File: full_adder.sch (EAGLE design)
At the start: 69 parts, among them IC1 SN74LS74AN, IC2 NE555, IC3 CD4052BE, IC4 CD4052BE, IC5 CD4052BE, IC6 74HC4051N,652

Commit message: reverse polarity protection added
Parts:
- added GND_IN, VCC_IN: LSP11, solpad:LSP11
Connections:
- new net N$30: VCC_IN.MP
- net GND: now also GND_IN.MP
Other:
- note added: "10 Reverse Polarity Protection"
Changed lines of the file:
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@@
 <part name="R21" library="rcl" library_urn="urn:adsk.eagle:library:334" deviceset="R-EU_" device="R1206" package3d_urn="urn:adsk.eagle:package:23540/2" value="1k"/>
 <part name="R22" library="rcl" library_urn="urn:adsk.eagle:library:334" deviceset="R-EU_" device="R1206" package3d_urn="urn:adsk.eagle:package:23540/2" value="1k"/>
+<part name="FRAME1" library="frames" library_urn="urn:adsk.eagle:library:229" deviceset="A3L-LOC" device=""/>
+<part name="VCC_IN" library="solpad" library_urn="urn:adsk.eagle:library:364" deviceset="LSP11" device="" package3d_urn="urn:adsk.eagle:package:26502/1"/>
+<part name="GND_IN" library="solpad" library_urn="urn:adsk.eagle:library:364" deviceset="LSP11" device="" package3d_urn="urn:adsk.eagle:package:26502/1"/>
+<part name="GND47" library="supply1" library_urn="urn:adsk.eagle:library:371" deviceset="GND" device=""/>
+<part name="Q1" library="transistor-power" library_urn="urn:adsk.eagle:library:400" deviceset="P-MOSFET_SYMBOL" device=""/>
 </parts>
 <sheets>
@@
 </segment>
 </net>
+</nets>
+</sheet>
+<sheet>
+<plain>
+<text x="-177.8" y="190.5" size="3.81" layer="100">10 Reverse Polarity Protection</text>
+</plain>
+<instances>
+<instance part="FRAME1" gate="G$1" x="-187.96" y="-55.88" smashed="yes">
+<attribute name="DRAWING_NAME" x="156.21" y="-40.64" size="2.54" layer="94"/>
+<attribute name="LAST_DATE_TIME" x="156.21" y="-45.72" size="2.286" layer="94"/>
+<attribute name="SHEET" x="169.545" y="-50.8" size="2.54" layer="94"/>
+</instance>
+<instance part="VCC_IN" gate="1" x="-170.18" y="177.8" smashed="yes" rot="R90">
+<attribute name="NAME" x="-168.91" y="182.499" size="1.778" layer="95" rot="R180"/>
+</instance>
+<instance part="GND_IN" gate="1" x="-170.18" y="162.56" smashed="yes" rot="R90">
+<attribute name="NAME" x="-168.91" y="167.259" size="1.778" layer="95" rot="R180"/>
+</instance>
+<instance part="GND47" gate="1" x="-149.86" y="157.48" smashed="yes">
+<attribute name="VALUE" x="-152.4" y="154.94" size="1.778" layer="96"/>
+</instance>
+<instance part="Q1" gate="G$1" x="-152.4" y="175.26" smashed="yes" rot="MR90">
+<attribute name="NAME" x="-152.4" y="182.88" size="1.778" layer="95" rot="MR180"/>
+<attribute name="VALUE" x="-152.4" y="185.42" size="1.778" layer="96" rot="MR180"/>
+</instance>
+</instances>
+<busses>
+</busses>
+<nets>
+<net name="N$30" class="0">
+<segment>
+<pinref part="VCC_IN" gate="1" pin="MP"/>
+<wire x1="-167.64" y1="177.8" x2="-157.48" y2="177.8" width="0.1524" layer="91"/>
+</segment>
+</net>
+<net name="VCC" class="0">
+<segment>
+<wire x1="-147.32" y1="177.8" x2="-144.78" y2="177.8" width="0.1524" layer="91"/>
+<label x="-144.78" y="177.8" size="1.016" layer="95" xref="yes"/>
+</segment>
+</net>
+<net name="GND" class="0">
+<segment>
+<pinref part="GND_IN" gate="1" pin="MP"/>
+<wire x1="-149.86" y1="172.72" x2="-149.86" y2="162.56" width="0.1524" layer="91"/>
+<wire x1="-149.86" y1="162.56" x2="-167.64" y2="162.56" width="0.1524" layer="91"/>
+<pinref part="GND47" gate="1" pin="GND"/>
+<wire x1="-149.86" y1="160.02" x2="-149.86" y2="162.56" width="0.1524" layer="91"/>
+<junction x="-149.86" y="162.56"/>
+</segment>
+</net>

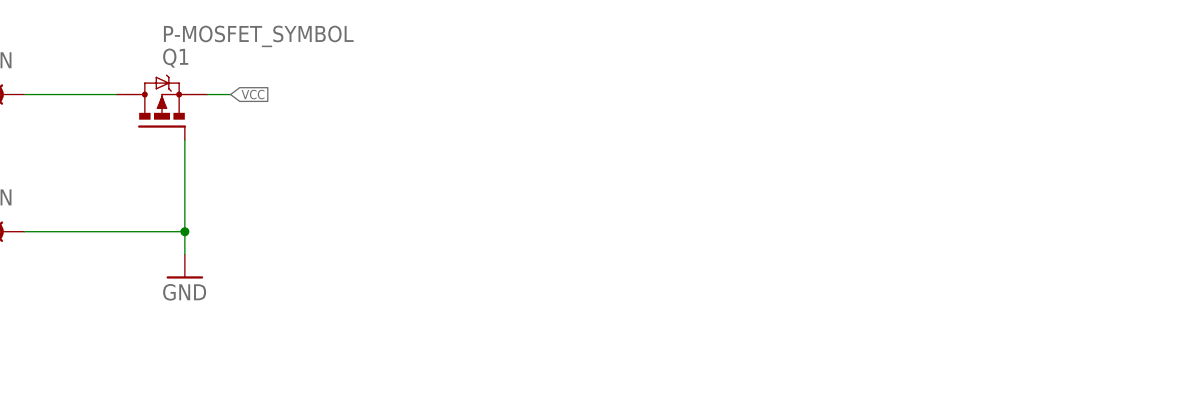
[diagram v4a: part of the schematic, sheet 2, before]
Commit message: basic input protection concept added
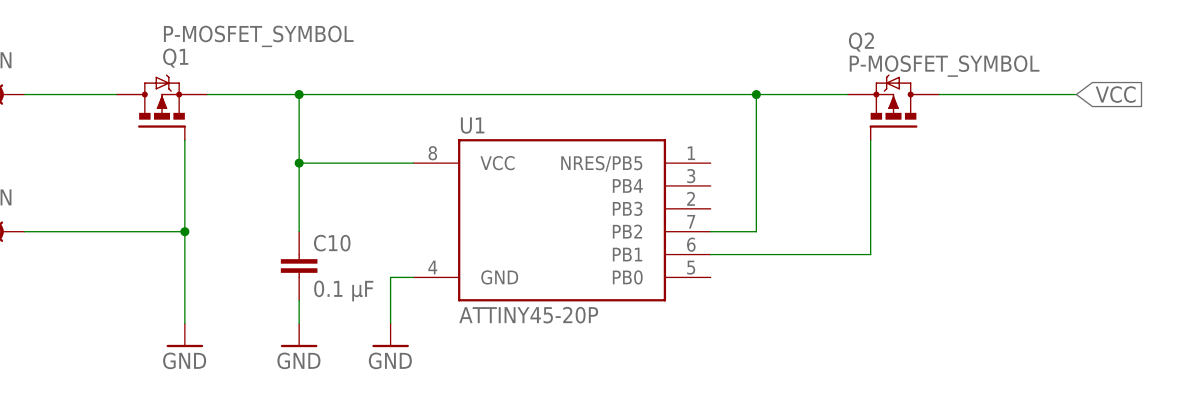
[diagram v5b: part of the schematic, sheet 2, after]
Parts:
- added C10: 0.1 µF, rcl:C-EU025-024X044
- added U1: ATTINY45-20P, _hhn_attiny25_45_85:ATTINY45-20P
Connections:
- new net N$31: C10.1, U1.PB2, U1.VCC
- new net N$32: U1.PB1
- net GND: now also C10.2, U1.GND
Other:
- note added: "10 Reverse Polarity + Overdischarge Protection"
- note removed: "10 Reverse Polarity Protection"
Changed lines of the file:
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@@
 <part name="GND47" library="supply1" library_urn="urn:adsk.eagle:library:371" deviceset="GND" device=""/>
 <part name="Q1" library="transistor-power" library_urn="urn:adsk.eagle:library:400" deviceset="P-MOSFET_SYMBOL" device=""/>
+<part name="U1" library="_hhn_attiny25_45_85" deviceset="ATTINY45*" device="P" technology="-20"/>
+<part name="GND48" library="supply1" library_urn="urn:adsk.eagle:library:371" deviceset="GND" device=""/>
+<part name="C10" library="rcl" library_urn="urn:adsk.eagle:library:334" deviceset="C-EU" device="025-024X044" package3d_urn="urn:adsk.eagle:package:23630/1" value="0.1 µF"/>
+<part name="GND49" library="supply1" library_urn="urn:adsk.eagle:library:371" deviceset="GND" device=""/>
+<part name="Q2" library="transistor-power" library_urn="urn:adsk.eagle:library:400" deviceset="P-MOSFET_SYMBOL" device=""/>
 </parts>
 <sheets>
@@
 <sheet>
 <plain>
-<text x="-177.8" y="190.5" size="3.81" layer="100">10 Reverse Polarity Protection</text>
+<text x="-177.8" y="190.5" size="3.81" layer="100">10 Reverse Polarity + Overdischarge Protection</text>
 </plain>
 <instances>
@@
 <attribute name="NAME" x="-168.91" y="167.259" size="1.778" layer="95" rot="R180"/>
 </instance>
-<instance part="GND47" gate="1" x="-149.86" y="157.48" smashed="yes">
-<attribute name="VALUE" x="-152.4" y="154.94" size="1.778" layer="96"/>
+<instance part="GND47" gate="1" x="-149.86" y="149.86" smashed="yes">
+<attribute name="VALUE" x="-152.4" y="147.32" size="1.778" layer="96"/>
 </instance>
 <instance part="Q1" gate="G$1" x="-152.4" y="175.26" smashed="yes" rot="MR90">
 <attribute name="NAME" x="-152.4" y="182.88" size="1.778" layer="95" rot="MR180"/>
 <attribute name="VALUE" x="-152.4" y="185.42" size="1.778" layer="96" rot="MR180"/>
+</instance>
+<instance part="U1" gate="G$1" x="-109.22" y="165.1" smashed="yes">
+<attribute name="NAME" x="-119.38" y="173.482" size="1.778" layer="95"/>
+<attribute name="VALUE" x="-119.38" y="152.4" size="1.778" layer="96"/>
+</instance>
+<instance part="GND48" gate="1" x="-127" y="149.86" smashed="yes">
+<attribute name="VALUE" x="-129.54" y="147.32" size="1.778" layer="96"/>
+</instance>
+<instance part="C10" gate="G$1" x="-137.16" y="160.02" smashed="yes">
+<attribute name="NAME" x="-135.636" y="160.401" size="1.778" layer="95"/>
+<attribute name="VALUE" x="-135.636" y="155.321" size="1.778" layer="96"/>
+</instance>
+<instance part="GND49" gate="1" x="-137.16" y="149.86" smashed="yes">
+<attribute name="VALUE" x="-139.7" y="147.32" size="1.778" layer="96"/>
+</instance>
+<instance part="Q2" gate="G$1" x="-71.12" y="175.26" smashed="yes" rot="R90">
+<attribute name="NAME" x="-76.2" y="182.88" size="1.778" layer="95"/>
+<attribute name="VALUE" x="-76.2" y="180.34" size="1.778" layer="96"/>
 </instance>
 </instances>
@@
 </segment>
 </net>
-<net name="VCC" class="0">
-<segment>
-<wire x1="-147.32" y1="177.8" x2="-144.78" y2="177.8" width="0.1524" layer="91"/>
-<label x="-144.78" y="177.8" size="1.016" layer="95" xref="yes"/>
-</segment>
-</net>
 <net name="GND" class="0">
 <segment>
@@
 <wire x1="-149.86" y1="162.56" x2="-167.64" y2="162.56" width="0.1524" layer="91"/>
 <pinref part="GND47" gate="1" pin="GND"/>
-<wire x1="-149.86" y1="160.02" x2="-149.86" y2="162.56" width="0.1524" layer="91"/>
+<wire x1="-149.86" y1="152.4" x2="-149.86" y2="162.56" width="0.1524" layer="91"/>
 <junction x="-149.86" y="162.56"/>
 </segment>
-</net>
+<segment>
+<pinref part="U1" gate="G$1" pin="GND"/>
+<wire x1="-124.46" y1="157.48" x2="-127" y2="157.48" width="0.1524" layer="91"/>
+<wire x1="-127" y1="157.48" x2="-127" y2="152.4" width="0.1524" layer="91"/>
+<pinref part="GND48" gate="1" pin="GND"/>
+</segment>
+<segment>
+<pinref part="GND49" gate="1" pin="GND"/>
+<pinref part="C10" gate="G$1" pin="2"/>
+<wire x1="-137.16" y1="152.4" x2="-137.16" y2="154.94" width="0.1524" layer="91"/>
+</segment>
+</net>
+<net name="N$31" class="0">
+<segment>
+<wire x1="-147.32" y1="177.8" x2="-137.16" y2="177.8" width="0.1524" layer="91"/>
+<pinref part="U1" gate="G$1" pin="VCC"/>
+<wire x1="-137.16" y1="177.8" x2="-137.16" y2="170.18" width="0.1524" layer="91"/>
+<wire x1="-137.16" y1="170.18" x2="-124.46" y2="170.18" width="0.1524" layer="91"/>
+<wire x1="-137.16" y1="177.8" x2="-86.36" y2="177.8" width="0.1524" layer="91"/>
+<wire x1="-86.36" y1="177.8" x2="-86.36" y2="162.56" width="0.1524" layer="91"/>
+<junction x="-137.16" y="177.8"/>
+<pinref part="U1" gate="G$1" pin="PB2"/>
+<wire x1="-86.36" y1="162.56" x2="-91.44" y2="162.56" width="0.1524" layer="91"/>
+<pinref part="C10" gate="G$1" pin="1"/>
+<wire x1="-137.16" y1="162.56" x2="-137.16" y2="170.18" width="0.1524" layer="91"/>
+<junction x="-137.16" y="170.18"/>
+<wire x1="-86.36" y1="177.8" x2="-76.2" y2="177.8" width="0.1524" layer="91"/>
+<junction x="-86.36" y="177.8"/>
+</segment>
+</net>
+<net name="N$32" class="0">
+<segment>
+<pinref part="U1" gate="G$1" pin="PB1"/>
+<wire x1="-91.44" y1="160.02" x2="-73.66" y2="160.02" width="0.1524" layer="91"/>
+<wire x1="-73.66" y1="172.72" x2="-73.66" y2="160.02" width="0.1524" layer="91"/>
+</segment>
+</net>
+<net name="VCC" class="0">
+<segment>
+<wire x1="-66.04" y1="177.8" x2="-50.8" y2="177.8" width="0.1524" layer="91"/>
+<label x="-50.8" y="177.8" size="1.778" layer="95" xref="yes"/>
+</segment>
+</net>

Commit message: minor fixes
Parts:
- added LED13: (no value), led:LED5MM
- added R23: 10k, rcl:R-EU_R1206
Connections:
- new net N$33: LED13.A, R23.1
- new net N$34: R23.2, U1.PB2
- net GND: now also LED13.C
- net N$31: no longer U1.PB2
- net N$32: now also U1.PB4; no longer U1.PB1
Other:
- note added: "small led"
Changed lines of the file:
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@@
 <part name="C10" library="rcl" library_urn="urn:adsk.eagle:library:334" deviceset="C-EU" device="025-024X044" package3d_urn="urn:adsk.eagle:package:23630/1" value="0.1 µF"/>
 <part name="GND49" library="supply1" library_urn="urn:adsk.eagle:library:371" deviceset="GND" device=""/>
-<part name="Q2" library="transistor-power" library_urn="urn:adsk.eagle:library:400" deviceset="P-MOSFET_SYMBOL" device=""/>
+<part name="Q3" library="transistor-power" library_urn="urn:adsk.eagle:library:400" deviceset="N-MOSFET_SYMBOL" device=""/>
+<part name="LED13" library="led" library_urn="urn:adsk.eagle:library:259" deviceset="LED" device="5MM" package3d_urn="urn:adsk.eagle:package:15799/2"/>
+<part name="R23" library="rcl" library_urn="urn:adsk.eagle:library:334" deviceset="R-EU_" device="R1206" package3d_urn="urn:adsk.eagle:package:23540/2" value="10k"/>
+<part name="GND50" library="supply1" library_urn="urn:adsk.eagle:library:371" deviceset="GND" device=""/>
 </parts>
 <sheets>
@@
 <plain>
 <text x="-177.8" y="190.5" size="3.81" layer="100">10 Reverse Polarity + Overdischarge Protection</text>
+<text x="-73.66" y="144.78" size="1.778" layer="97">small led</text>
 </plain>
 <instances>
@@
 <attribute name="NAME" x="-168.91" y="167.259" size="1.778" layer="95" rot="R180"/>
 </instance>
-<instance part="GND47" gate="1" x="-149.86" y="149.86" smashed="yes">
-<attribute name="VALUE" x="-152.4" y="147.32" size="1.778" layer="96"/>
+<instance part="GND47" gate="1" x="-149.86" y="139.7" smashed="yes">
+<attribute name="VALUE" x="-152.4" y="137.16" size="1.778" layer="96"/>
 </instance>
 <instance part="Q1" gate="G$1" x="-152.4" y="175.26" smashed="yes" rot="MR90">
@@
 <attribute name="VALUE" x="-119.38" y="152.4" size="1.778" layer="96"/>
 </instance>
-<instance part="GND48" gate="1" x="-127" y="149.86" smashed="yes">
-<attribute name="VALUE" x="-129.54" y="147.32" size="1.778" layer="96"/>
+<instance part="GND48" gate="1" x="-127" y="139.7" smashed="yes">
+<attribute name="VALUE" x="-129.54" y="137.16" size="1.778" layer="96"/>
 </instance>
 <instance part="C10" gate="G$1" x="-137.16" y="160.02" smashed="yes">
@@
 <attribute name="VALUE" x="-135.636" y="155.321" size="1.778" layer="96"/>
 </instance>
-<instance part="GND49" gate="1" x="-137.16" y="149.86" smashed="yes">
-<attribute name="VALUE" x="-139.7" y="147.32" size="1.778" layer="96"/>
-</instance>
-<instance part="Q2" gate="G$1" x="-71.12" y="175.26" smashed="yes" rot="R90">
-<attribute name="NAME" x="-76.2" y="182.88" size="1.778" layer="95"/>
-<attribute name="VALUE" x="-76.2" y="180.34" size="1.778" layer="96"/>
+<instance part="GND49" gate="1" x="-137.16" y="139.7" smashed="yes">
+<attribute name="VALUE" x="-139.7" y="137.16" size="1.778" layer="96"/>
+</instance>
+<instance part="Q3" gate="G$1" x="-81.28" y="175.26" smashed="yes" rot="R90">
+<attribute name="NAME" x="-86.36" y="182.88" size="1.778" layer="95"/>
+<attribute name="VALUE" x="-86.36" y="180.34" size="1.778" layer="96"/>
+</instance>
+<instance part="LED13" gate="G$1" x="-78.74" y="147.32" smashed="yes">
+<attribute name="NAME" x="-75.184" y="142.748" size="1.778" layer="95" rot="R90"/>
+<attribute name="VALUE" x="-73.025" y="142.748" size="1.778" layer="96" rot="R90"/>
+</instance>
+<instance part="R23" gate="G$1" x="-78.74" y="154.94" smashed="yes" rot="R90">
+<attribute name="NAME" x="-77.47" y="156.4386" size="1.778" layer="95"/>
+<attribute name="VALUE" x="-77.47" y="154.178" size="1.778" layer="96"/>
+</instance>
+<instance part="GND50" gate="1" x="-78.74" y="139.7" smashed="yes">
+<attribute name="VALUE" x="-81.28" y="137.16" size="1.778" layer="96"/>
 </instance>
 </instances>
@@
 <wire x1="-149.86" y1="162.56" x2="-167.64" y2="162.56" width="0.1524" layer="91"/>
 <pinref part="GND47" gate="1" pin="GND"/>
-<wire x1="-149.86" y1="152.4" x2="-149.86" y2="162.56" width="0.1524" layer="91"/>
+<wire x1="-149.86" y1="142.24" x2="-149.86" y2="162.56" width="0.1524" layer="91"/>
 <junction x="-149.86" y="162.56"/>
 </segment>
@@
 <pinref part="U1" gate="G$1" pin="GND"/>
 <wire x1="-124.46" y1="157.48" x2="-127" y2="157.48" width="0.1524" layer="91"/>
-<wire x1="-127" y1="157.48" x2="-127" y2="152.4" width="0.1524" layer="91"/>
+<wire x1="-127" y1="157.48" x2="-127" y2="142.24" width="0.1524" layer="91"/>
 <pinref part="GND48" gate="1" pin="GND"/>
 </segment>
@@
 <pinref part="GND49" gate="1" pin="GND"/>
 <pinref part="C10" gate="G$1" pin="2"/>
-<wire x1="-137.16" y1="152.4" x2="-137.16" y2="154.94" width="0.1524" layer="91"/>
+<wire x1="-137.16" y1="142.24" x2="-137.16" y2="154.94" width="0.1524" layer="91"/>
+</segment>
+<segment>
+<pinref part="GND50" gate="1" pin="GND"/>
+<pinref part="LED13" gate="G$1" pin="C"/>
 </segment>
 </net>
@@
 <wire x1="-137.16" y1="170.18" x2="-124.46" y2="170.18" width="0.1524" layer="91"/>
 <wire x1="-137.16" y1="177.8" x2="-86.36" y2="177.8" width="0.1524" layer="91"/>
-<wire x1="-86.36" y1="177.8" x2="-86.36" y2="162.56" width="0.1524" layer="91"/>
 <junction x="-137.16" y="177.8"/>
-<pinref part="U1" gate="G$1" pin="PB2"/>
-<wire x1="-86.36" y1="162.56" x2="-91.44" y2="162.56" width="0.1524" layer="91"/>
 <pinref part="C10" gate="G$1" pin="1"/>
 <wire x1="-137.16" y1="162.56" x2="-137.16" y2="170.18" width="0.1524" layer="91"/>
 <junction x="-137.16" y="170.18"/>
-<wire x1="-86.36" y1="177.8" x2="-76.2" y2="177.8" width="0.1524" layer="91"/>
-<junction x="-86.36" y="177.8"/>
+</segment>
+</net>
+<net name="VCC" class="0">
+<segment>
+<wire x1="-76.2" y1="177.8" x2="-58.42" y2="177.8" width="0.1524" layer="91"/>
+<label x="-58.42" y="177.8" size="1.778" layer="95" xref="yes"/>
 </segment>
 </net>
 <net name="N$32" class="0">
 <segment>
-<pinref part="U1" gate="G$1" pin="PB1"/>
-<wire x1="-91.44" y1="160.02" x2="-73.66" y2="160.02" width="0.1524" layer="91"/>
-<wire x1="-73.66" y1="172.72" x2="-73.66" y2="160.02" width="0.1524" layer="91"/>
-</segment>
-</net>
-<net name="VCC" class="0">
-<segment>
-<wire x1="-66.04" y1="177.8" x2="-50.8" y2="177.8" width="0.1524" layer="91"/>
-<label x="-50.8" y="177.8" size="1.778" layer="95" xref="yes"/>
-</segment>
-</net>
+<pinref part="U1" gate="G$1" pin="PB4"/>
+<wire x1="-91.44" y1="167.64" x2="-78.74" y2="167.64" width="0.1524" layer="91"/>
+<wire x1="-78.74" y1="167.64" x2="-78.74" y2="172.72" width="0.1524" layer="91"/>
+</segment>
+</net>
+<net name="N$33" class="0">
+<segment>
+<pinref part="R23" gate="G$1" pin="1"/>
+<pinref part="LED13" gate="G$1" pin="A"/>
+</segment>
+</net>
+<net name="N$34" class="0">
+<segment>
+<pinref part="U1" gate="G$1" pin="PB2"/>
+<wire x1="-91.44" y1="162.56" x2="-78.74" y2="162.56" width="0.1524" layer="91"/>
+<pinref part="R23" gate="G$1" pin="2"/>
+<wire x1="-78.74" y1="162.56" x2="-78.74" y2="160.02" width="0.1524" layer="91"/>
+</segment>
+</net>
